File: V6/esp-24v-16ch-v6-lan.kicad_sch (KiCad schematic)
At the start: 31 parts, among them J8 ETHERNET, U5 LAN8710A

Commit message: Cleanup
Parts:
- R20: value 10k -> 1.5k; LCSC Part # C25744 -> C25867; Mfr PN 0402WGF1002TCE -> 0402WGF1501TCE; Vendor PN C25744 -> C25867
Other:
- note added: "FOR NEXT VERSION: REMOVE MODE PULL-UPS (THERE ARE INTERNAL PULL-UPS) REMOVE ADDRESS PULL-DOWNS (THERE ARE INTERNAL PULL-DOWNS) INSTALL ONE SINGLE PULL-UP ON PIN 13 (/PHYAD0) TO SELECT ADDRESS 1 AS SUGGESTED IN THE DATASHEET."
- moved on the sheet: C22, R30, TP16, TP17

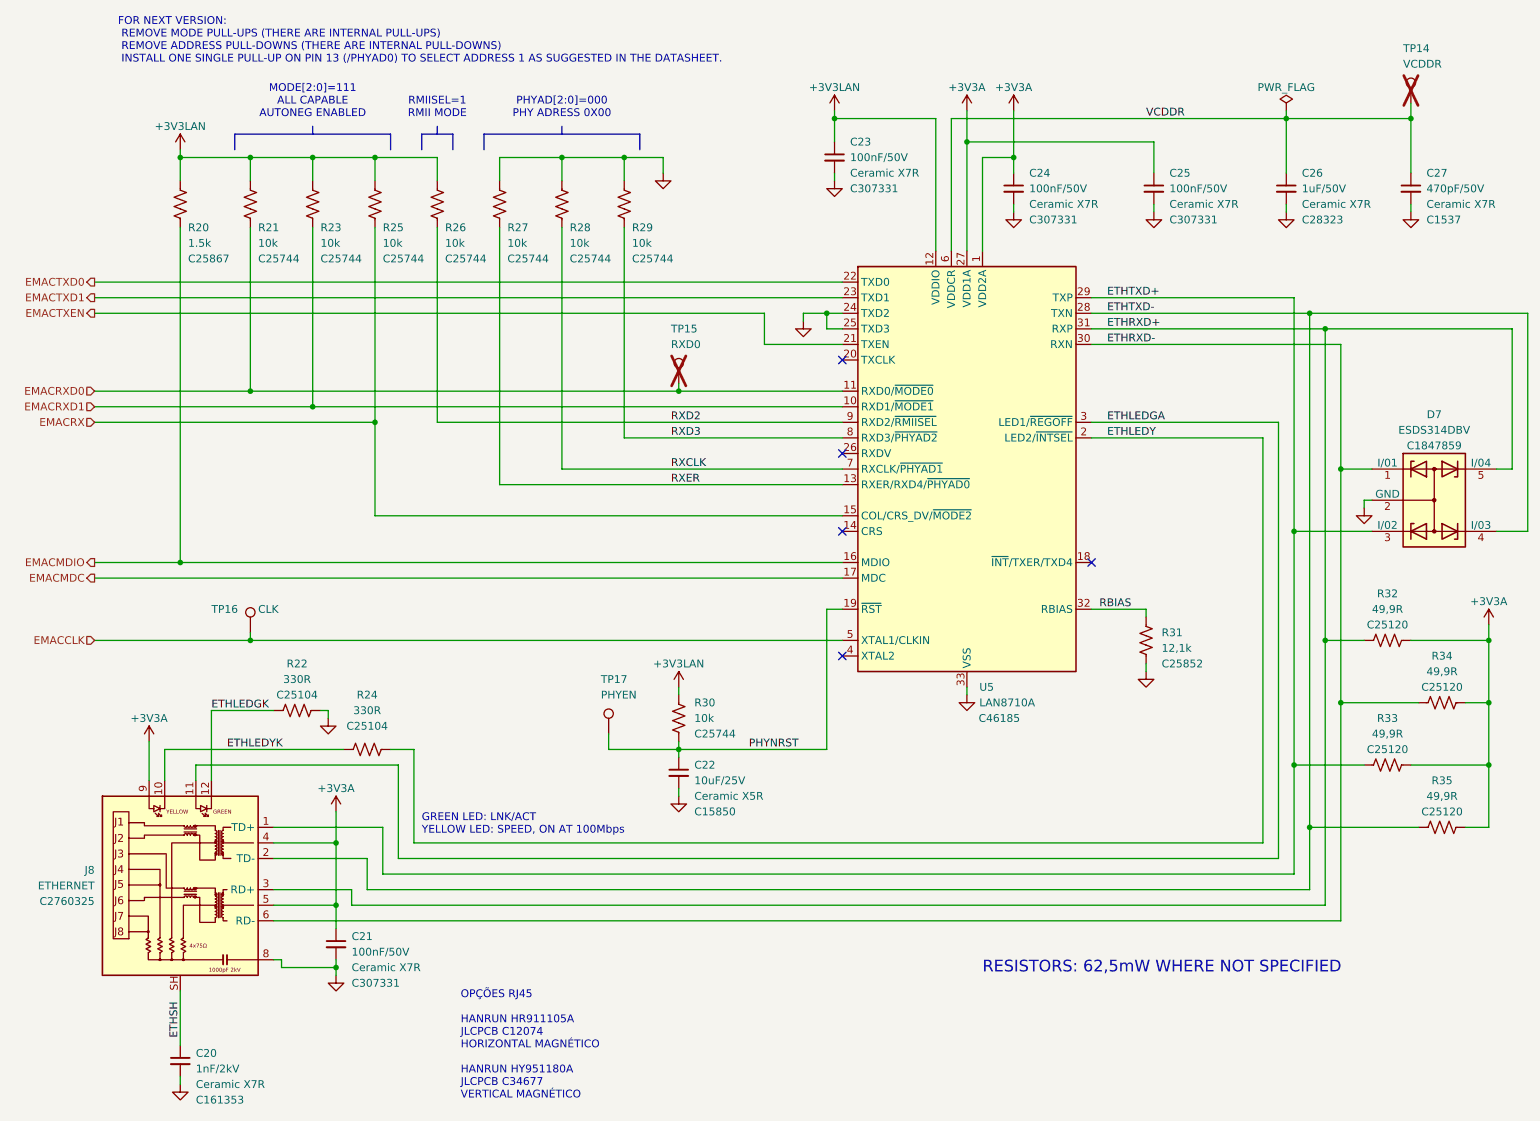
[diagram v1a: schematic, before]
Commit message: Update resistance value for pull-ups.
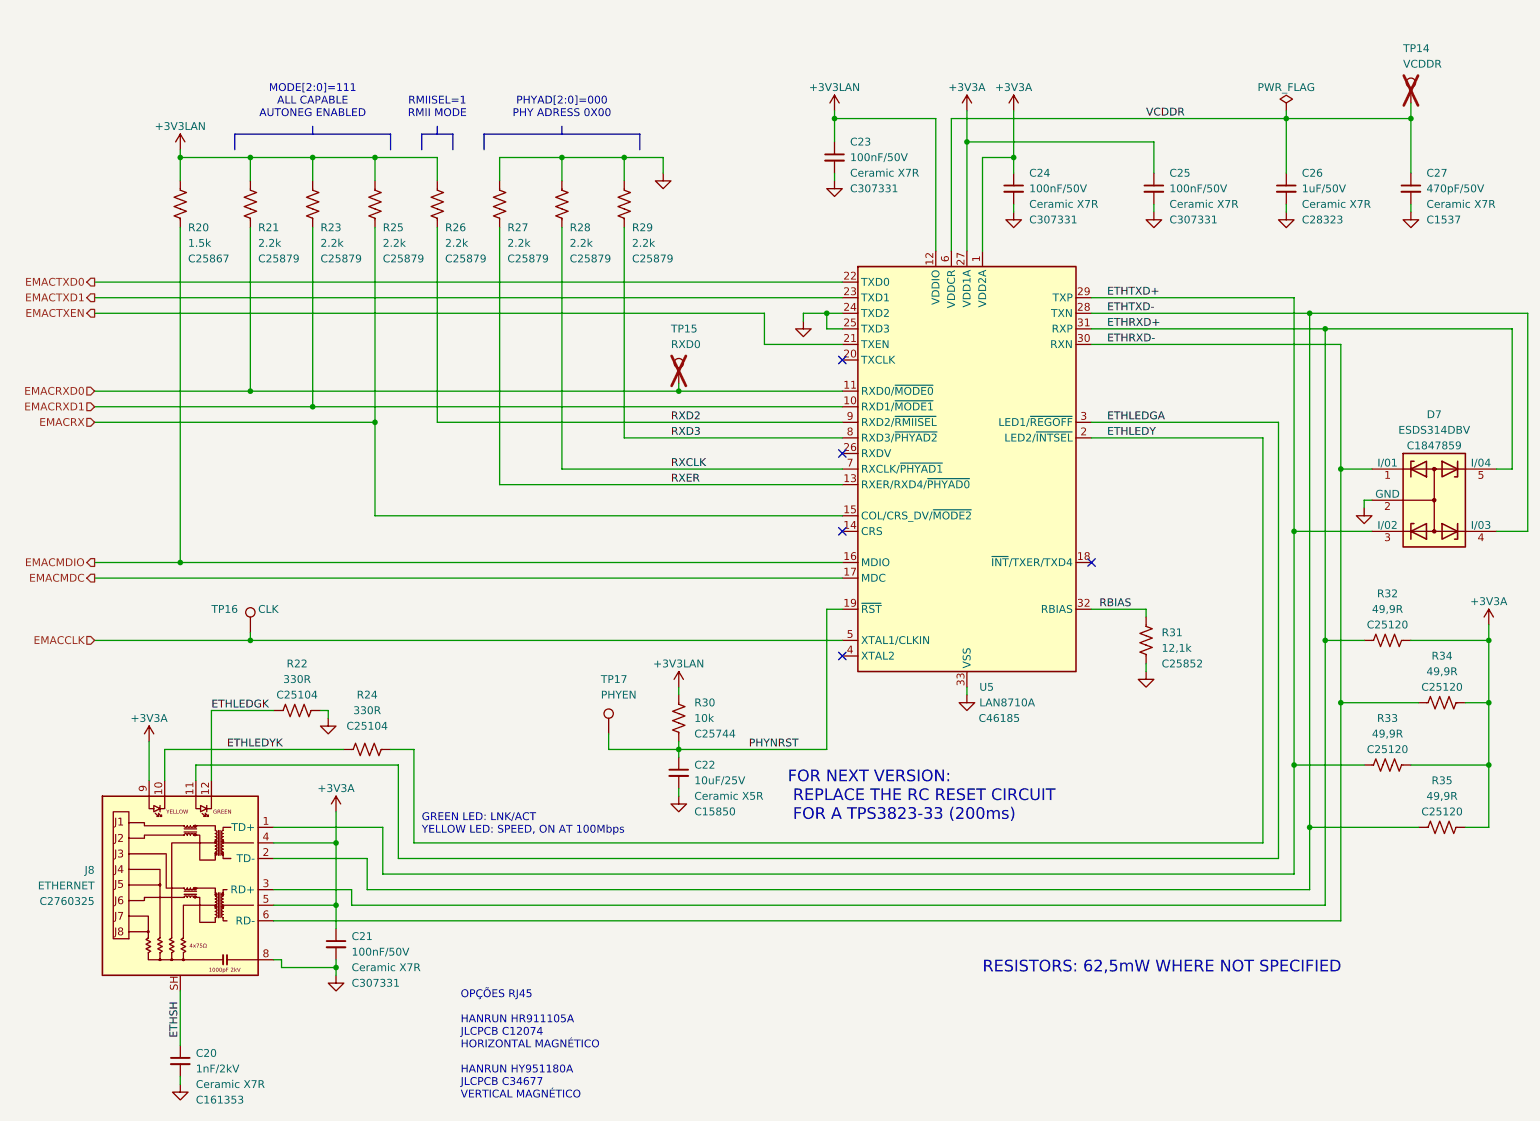
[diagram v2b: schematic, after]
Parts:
- R21: value 10k -> 2.2k; LCSC Part # C25744 -> C25879; Mfr PN 0402WGF1002TCE -> 0402WGF2201TCE; Vendor PN C25744 -> C25879
- R23, R25, R26, R27, R28, R29: value 10k -> 2.2k; LCSC Part # C25744 -> C25879; Mfr PN 0402WGF1002TCE -> 0402WGF2201TCE
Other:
- note added: "FOR NEXT VERSION: REPLACE THE RC RESET CIRCUIT FOR A TPS3823-33 (200ms)"
- note removed: "FOR NEXT VERSION: REMOVE MODE PULL-UPS (THERE ARE INTERNAL PULL-UPS) REMOVE ADDRESS PULL-DOWNS (THERE ARE INTERNAL PULL-DOWNS) INSTALL ONE SINGLE PULL-UP ON PIN 13 (/PHYAD0) TO SELECT ADDRESS 1 AS SUGGESTED IN THE DATASHEET."
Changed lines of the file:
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@@
 		(rev "V6.0")
 	)
-	(text "FOR NEXT VERSION:\n REMOVE MODE PULL-UPS (THERE ARE INTERNAL PULL-UPS)\n REMOVE ADDRESS PULL-DOWNS (THERE ARE INTERNAL PULL-DOWNS)\n INSTALL ONE SINGLE PULL-UP ON PIN 13 (/PHYAD0) TO SELECT ADDRESS 1 AS SUGGESTED IN THE DATASHEET."
+	(text "FOR NEXT VERSION:\n REPLACE THE RC RESET CIRCUIT\n FOR A TPS3823-33 (200ms)"
 		(exclude_from_sim no)
-		(at 38.1 19.05 0)
+		(at 147.32 142.24 0)
 		(effects
 			(font
-				(size 1.27 1.27)
+				(size 1.905 1.905)
 			)
 			(justify left)
@@
 			)
 		)
-		(property "Value" "10k"
+		(property "Value" "2.2k"
 			(at 81.28 52.07 0)
 			(show_name no)
@@
 			)
 		)
-		(property "Mfr PN" "0402WGF1002TCE"
+		(property "Mfr PN" "0402WGF2201TCE"
 			(at 80.01 45.72 0)
 			(hide yes)
@@
 			)
 		)
-		(property "LCSC Part #" "C25744"
+		(property "LCSC Part #" "C25879"
 			(at 81.28 54.61 0)
 			(show_name no)
@@
 			)
 		)
-		(property "Value" "10k"
+		(property "Value" "2.2k"
 			(at 91.44 52.07 0)
 			(show_name no)
@@
 			)
 		)
-		(property "Mfr PN" "0402WGF1002TCE"
+		(property "Mfr PN" "0402WGF2201TCE"
 			(at 90.17 45.72 0)
 			(hide yes)
@@
 			)
 		)
-		(property "LCSC Part #" "C25744"
+		(property "LCSC Part #" "C25879"
 			(at 91.44 54.61 0)
 			(show_name no)
@@
 			)
 		)
-		(property "Value" "10k"
+		(property "Value" "2.2k"
 			(at 121.92 52.07 0)
 			(show_name no)
@@
 			)
 		)
-		(property "Mfr PN" "0402WGF1002TCE"
+		(property "Mfr PN" "0402WGF2201TCE"
 			(at 120.65 45.72 0)
 			(hide yes)
@@
 			)
 		)
-		(property "LCSC Part #" "C25744"
+		(property "LCSC Part #" "C25879"
 			(at 121.92 54.61 0)
 			(show_name no)
@@
 			)
 		)
-		(property "Value" "10k"
+		(property "Value" "2.2k"
 			(at 71.12 52.07 0)
 			(show_name no)
@@
 			)
 		)
-		(property "Mfr PN" "0402WGF1002TCE"
+		(property "Mfr PN" "0402WGF2201TCE"
 			(at 69.85 45.72 0)
 			(hide yes)
@@
 			)
 		)
-		(property "LCSC Part #" "C25744"
+		(property "LCSC Part #" "C25879"
 			(at 71.12 54.61 0)
 			(show_name no)
@@
 			)
 		)
-		(property "Value" "10k"
+		(property "Value" "2.2k"
 			(at 111.76 52.07 0)
 			(show_name no)
@@
 			)
 		)
-		(property "Mfr PN" "0402WGF1002TCE"
+		(property "Mfr PN" "0402WGF2201TCE"
 			(at 110.49 45.72 0)
 			(hide yes)
@@
 			)
 		)
-		(property "LCSC Part #" "C25744"
+		(property "LCSC Part #" "C25879"
 			(at 111.76 54.61 0)
 			(show_name no)
@@
 			)
 		)
-		(property "Value" "10k"
+		(property "Value" "2.2k"
 			(at 60.96 52.07 0)
 			(show_name no)
@@
 			)
 		)
-		(property "Mfr PN" "0402WGF1002TCE"
+		(property "Mfr PN" "0402WGF2201TCE"
 			(at 59.69 45.72 0)
 			(hide yes)
@@
 			)
 		)
-		(property "Vendor PN" "C25744"
+		(property "Vendor PN" "C25879"
 			(at 59.69 45.72 0)
 			(hide yes)
@@
 			)
 		)
-		(property "LCSC Part #" "C25744"
+		(property "LCSC Part #" "C25879"
 			(at 60.96 54.61 0)
 			(show_name no)
@@
 			)
 		)
-		(property "Value" "10k"
+		(property "Value" "2.2k"
 			(at 101.6 52.07 0)
 			(show_name no)
@@
 			)
 		)
-		(property "Mfr PN" "0402WGF1002TCE"
+		(property "Mfr PN" "0402WGF2201TCE"
 			(at 100.33 45.72 0)
 			(hide yes)
@@
 			)
 		)
-		(property "LCSC Part #" "C25744"
+		(property "LCSC Part #" "C25879"
 			(at 101.6 54.61 0)
 			(show_name no)

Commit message: Added voltage monitors for both ESP32 and LAN8710A
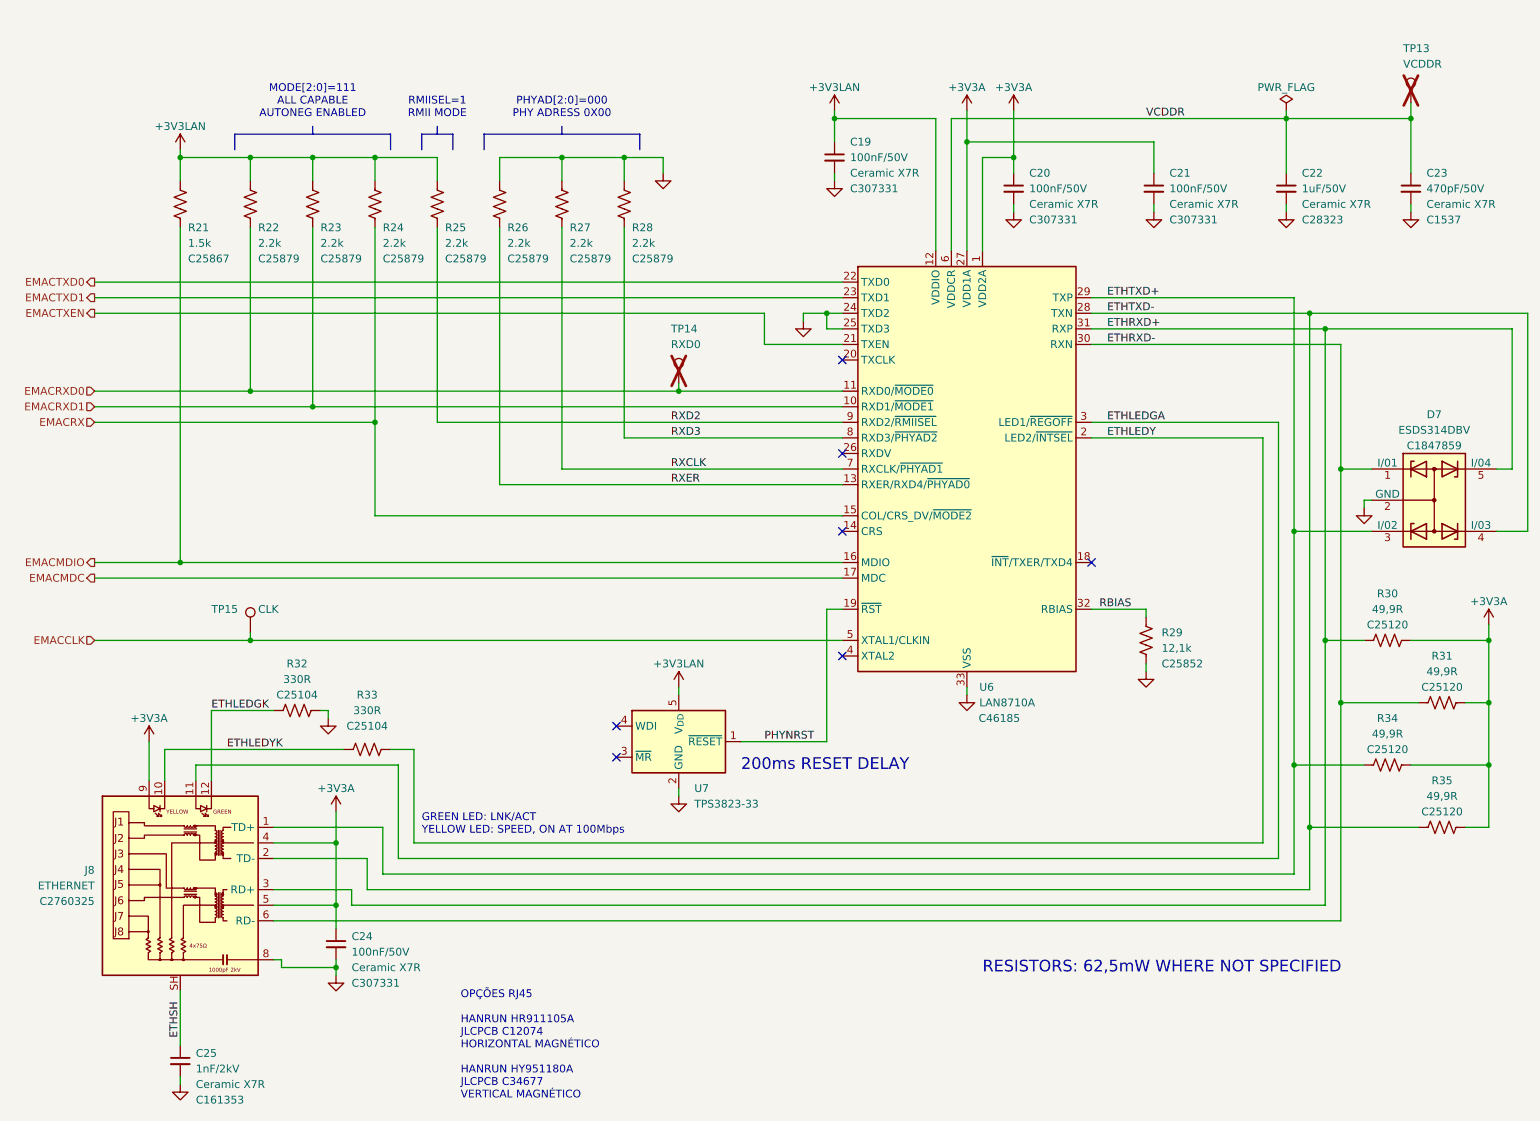
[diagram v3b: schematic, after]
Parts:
- removed C22: 10uF/25V, Tales:C_0805_2012Metric, symbol Device:C_Small
- removed R30: 10k, Tales:R_0402_1005Metric, symbol Device:R_US
- removed TP17: PHYEN, TestPoint:TestPoint_Pad_D1.5mm, symbol Connector:TestPoint
- added U7: TPS3823-33, Package_TO_SOT_SMD:SOT-23-5, symbol Power_Supervisor:TPS3823-xxDBV
- renumbered C23 to C19, C24 to C20, C25 to C21, C26 to C22, C27 to C23, C21 to C24, C20 to C25, R20 to R21, R21 to R22, R25 to R24, R26 to R25, R27 to R26, R28 to R27, R29 to R28, R31 to R29, R32 to R30, R34 to R31, R22 to R32, R24 to R33, R33 to R34, TP14 to TP13, TP15 to TP14, TP16 to TP15, U5 to U6
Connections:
- net +3V3LAN: now also U7.5 (V_{DD})
- net GND: now also U7.2 (GND)
- net PHYNRST: now also U7.1 (~{RESET})
- no-connect marks 5 -> 7
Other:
- note added: "200ms RESET DELAY"
- note removed: "FOR NEXT VERSION: REPLACE THE RC RESET CIRCUIT FOR A TPS3823-33 (200ms)"
